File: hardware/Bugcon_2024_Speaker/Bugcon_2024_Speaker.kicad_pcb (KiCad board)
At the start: 2 copper layers, 81.7 x 139.8 mm, 60 parts, among them J1 OLED, J2 Add_On, J4 Battery, J5 Battery, P1 USB_C_Plug_USB2.0, Q1 DMG3415U-7, SW1 ON, U1 ESP32-C6-WROOM-1U-N4, U2 XC6220B331MR-G

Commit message: feat(Hw):Update_Route_And_Labels
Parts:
- added kibuzzard-666C89F7: G***, kibuzzard-666C89F7, B.Cu at (146.4, 90.0)
- added kibuzzard-666C8A00: G***, kibuzzard-666C8A00, B.Cu at (109.2, 89.7)
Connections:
- J1 pad 1: /EN -> unconnected-(J1-Pin_1-Pad1)
- U1 pad 16: /SDAO -> /DOWN
- U1 pad 17: /DOWN -> /SDAO
- U1 pad 18: /SCLO -> /LEFT
- U1 pad 19: /LEFT -> /SCLO
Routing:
- net /EN: track 69.3 -> 49.0 mm, vias 1 -> 0
- net /LEFT: track 89.0 -> 87.7 mm
- net /DOWN: track 99.2 -> 98.2 mm
- net /SDAO: track 40.8 -> 39.9 mm
- net /SCLO: track 38.1 -> 38.9 mm

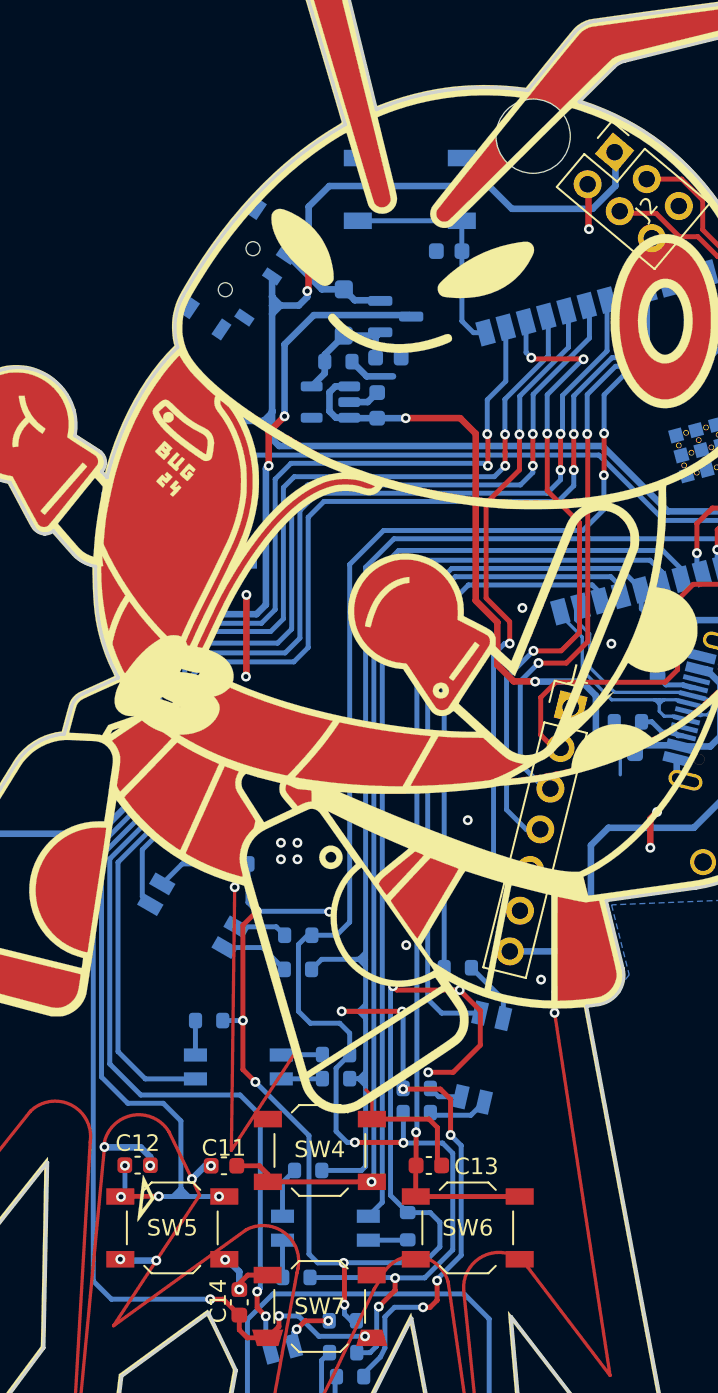
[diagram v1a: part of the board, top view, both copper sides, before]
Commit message: feat(Hw):Moved_Hole_Speaker
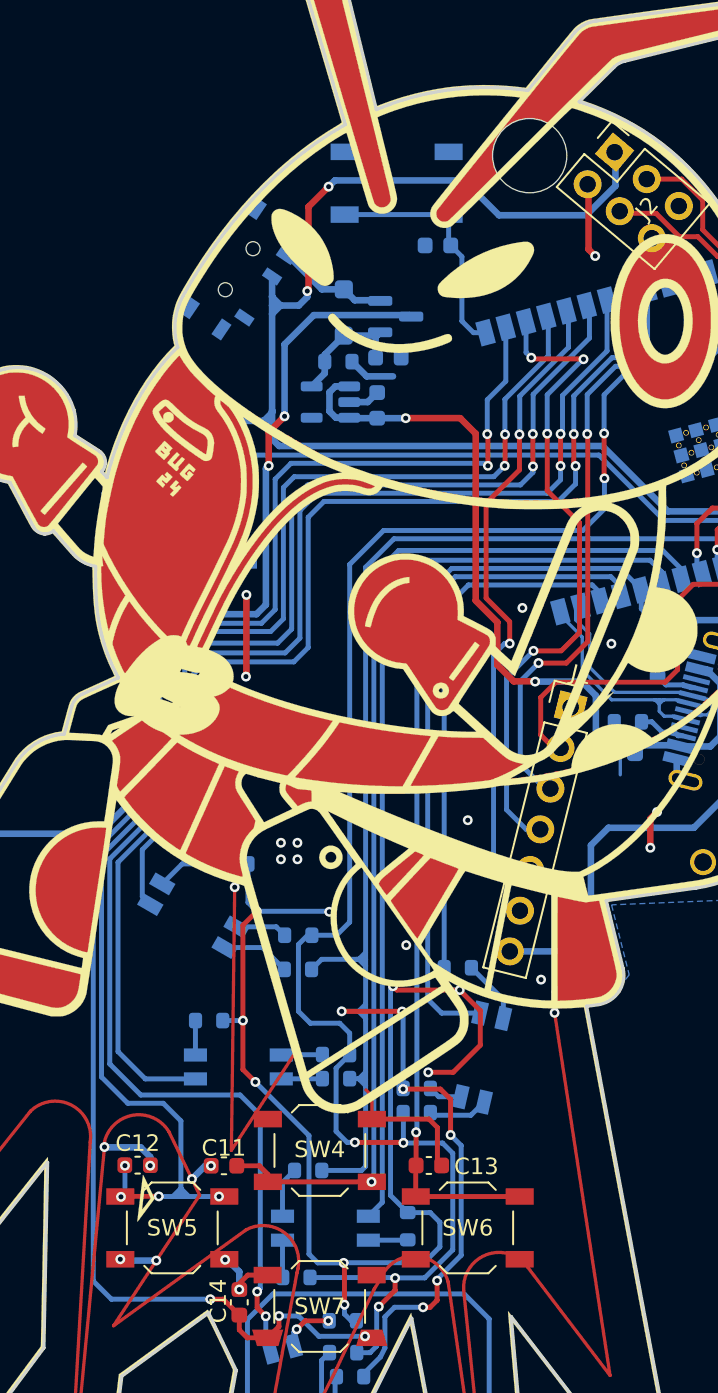
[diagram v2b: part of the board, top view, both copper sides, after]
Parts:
- moved ? 1.20 mm to (139.1, 51.4)
- moved SW2 0.88 mm to (131.0, 53.0)
- moved C6 0.76 mm to (133.5, 56.8)
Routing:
- net GND: track 315.0 -> 316.8 mm
- net /BOOT: track 14.1 -> 14.8 mm
- net /VOUT: track 130.1 -> 130.7 mm

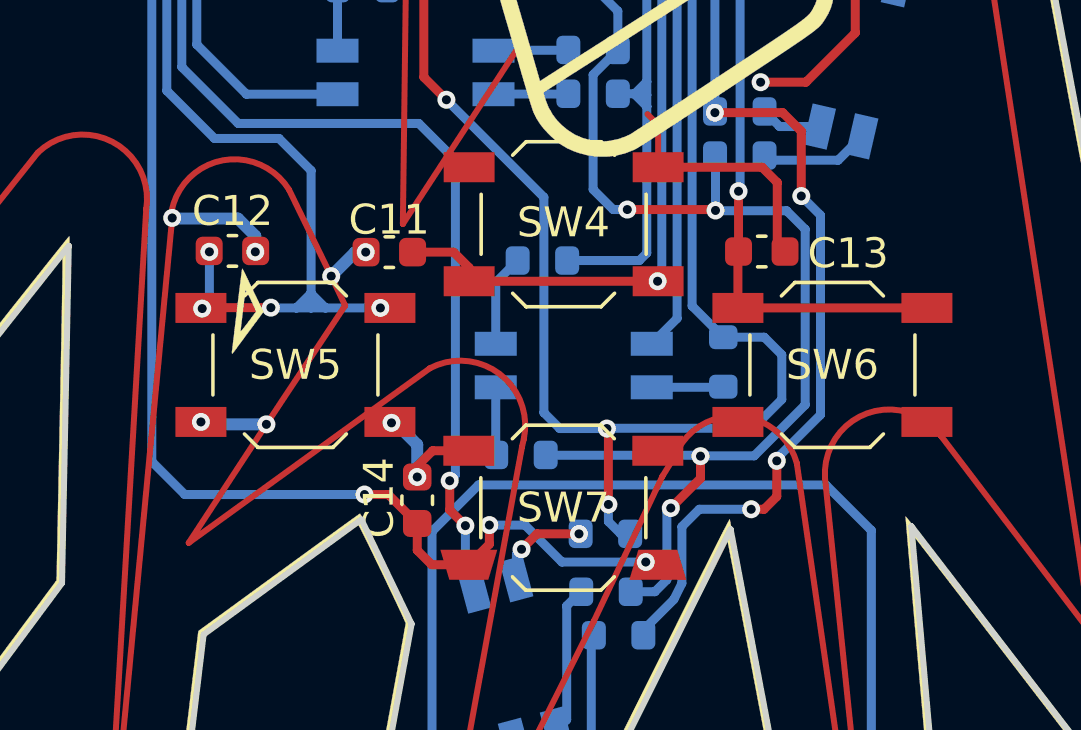
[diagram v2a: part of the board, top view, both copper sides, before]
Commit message: feat(Hw):Update_Labels
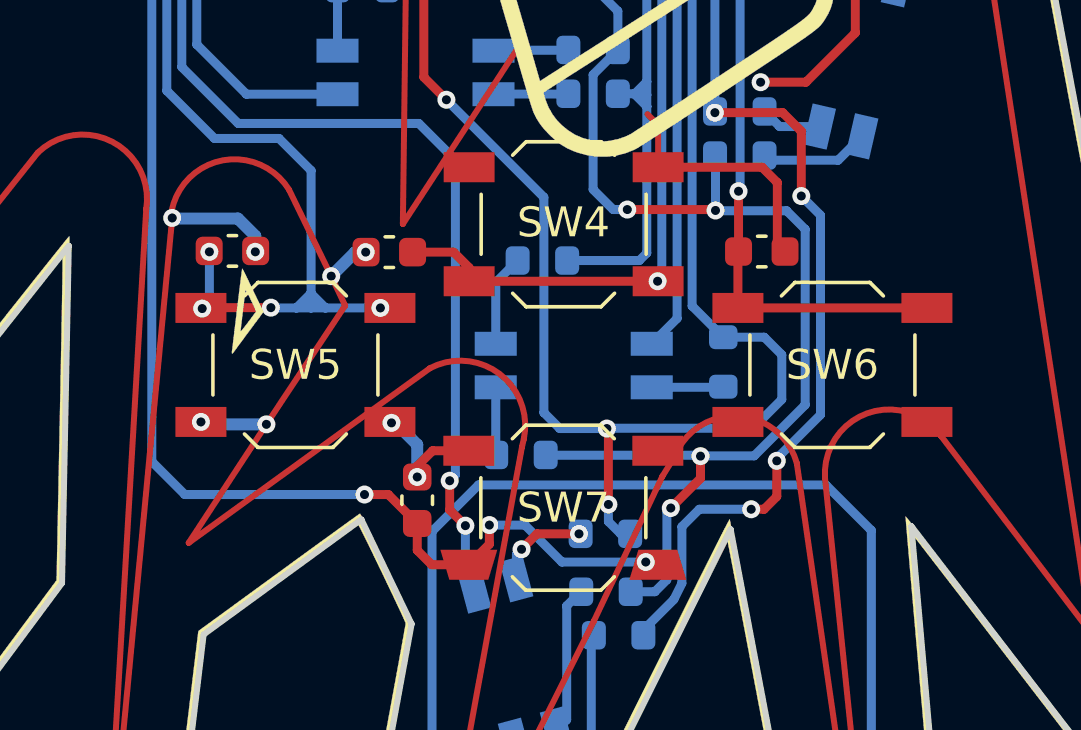
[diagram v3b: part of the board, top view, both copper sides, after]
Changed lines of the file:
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@@
 			(at -0.07957 1.27771 90)
 			(layer "F.SilkS")
+			(hide yes)
 			(effects
 				(font
@@
 			(at -0.00229 1.32957 0)
 			(layer "F.SilkS")
+			(hide yes)
 			(effects
 				(font
@@
 			(at -0.00771 -1.07957 0)
 			(layer "F.SilkS")
+			(hide yes)
 			(effects
 				(font
@@
 			(at -2.87729 -0.06043 0)
 			(layer "F.SilkS")
+			(hide yes)
 			(effects
 				(font
@@
 			(at 4.455 0 0)
 			(layer "B.SilkS")
+			(hide yes)
 			(effects
 				(font
@@
 			(at -5.02 0.01 0)
 			(layer "B.SilkS")
+			(hide yes)
 			(effects
 				(font
@@
 			(at -2.24 0.02 0)
 			(layer "B.SilkS")
+			(hide yes)
 			(effects
 				(font
@@
 		(tags "resistor")
 		(property "Reference" "R13"
-			(at 0 -2.53 0)
+			(at 0 -3.5 0)
 			(layer "B.SilkS")
 			(effects
@@
 			(at 0 1.43 0)
 			(layer "B.SilkS")
+			(hide yes)
 			(effects
 				(font
@@
 		(tags "resistor")
 		(property "Reference" "R16"
-			(at 0 -2.79 0)
+			(at 0 -3.8 0)
 			(layer "B.SilkS")
 			(effects
@@
 			(at 0.1 -1.4 0)
 			(layer "B.SilkS")
+			(hide yes)
 			(effects
 				(font
@@
 			(at -2.855 0 0)
 			(layer "B.SilkS")
+			(hide yes)
 			(effects
 				(font
@@
 			(at 4.533118 -0.404647 105)
 			(layer "B.SilkS")
+			(hide yes)
 			(effects
 				(font
@@
 			(at 0 1.43 0)
 			(layer "B.SilkS")
+			(hide yes)
 			(effects
 				(font
@@
 			(at 0 -1.51 90)
 			(layer "B.SilkS")
+			(hide yes)
 			(effects
 				(font
@@
 			(at -2.808577 2.132486 150)
 			(layer "B.SilkS")
+			(hide yes)
 			(effects
 				(font
@@
 			(at 0 1.3 0)
 			(layer "B.SilkS")
+			(hide yes)
 			(effects
 				(font
@@
 			(at 5.091223 -0.515376 77)
 			(layer "B.SilkS")
+			(hide yes)
 			(effects
 				(font
@@
 		(net 0)
 		(net_name "")
-		(layer "B.Cu")
+		(layers "F&B.Cu")
 		(hatch edge 0.5)
 		(connect_pads
@@
 		(polygon
 			(pts
-				(xy 148.45 63.48) (xy 148.45 59.28) (xy 146.17 59.28) (xy 146.17 63.48)
+				(xy 126.62 93.47) (xy 127.43 93.47) (xy 127.43 94.28) (xy 126.63 94.27)
 			)
 		)
@@
 		(polygon
 			(pts
-				(xy 126.62 93.47) (xy 127.43 93.47) (xy 127.43 94.28) (xy 126.63 94.27)
+				(xy 148.45 63.48) (xy 148.45 59.28) (xy 146.17 59.28) (xy 146.17 63.48)
 			)
 		)

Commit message: feat: add more labels
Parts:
- added kibuzzard-66FD9EC0: G***, kibuzzard-66FD9EC0, B.Cu at (142.1, 49.2)
- added kibuzzard-66FD9F77: G***, kibuzzard-66FD9F77, B.Cu at (129.4, 79.1)
- moved kibuzzard-66F1E462 1.87 mm to (138.1, 54.9)
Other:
- board text added: "Este es el final del camino gracias por acompañarnos LATAM El luchador, el dragon, la llama y BugCon te dan las gracias - Dijo el Gato"
- board text added: "Un VIP, un VIP!!"
- board text added: "github.com/ElectronicCats/ badge-bugcon-2024"

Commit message: feat(Hw):Update_Labels_And_route
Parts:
- added kibuzzard-670026B6: G***, kibuzzard-670026B6, B.Cu at (130.0, 96.5)
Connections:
- U1 pad 26: /DC -> /LED2
- U1 pad 27: /LED2 -> /DC
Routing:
- net /LED2: track 107.0 -> 106.1 mm
- net /DC: track 40.6 -> 41.3 mm
